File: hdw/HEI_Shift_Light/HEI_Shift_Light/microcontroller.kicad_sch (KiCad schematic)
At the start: 13 parts

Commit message: more schematic progress
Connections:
- net PIC18F_ICSPCLK: now also U?.13 (RA1)
- net PIC18F_ICSPDAT: now also U?.14 (RA0)
- net C2OUT: now reaches U?.10 (RC1)
- net TACH_PULSE: now reaches U?.11 (RC0)
- net TACH_ANALOG: now reaches U?.16 (RB5)
- net USB_UART_TX: now reaches U?.19 (RC7)
- net CLKR: now reaches U?.2 (RA5)
- net USB_UART_RX: now reaches U?.20 (RC6)
- net LED_R: now reaches U?.5 (RC5)
- net LED_G: now reaches U?.6 (RC4)
- net LED_B: now reaches U?.7 (RC3)
- net OPA1OUT: now reaches U?.9 (RC2)
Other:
- note added: "C2IN0+"
- note added: "C2OUT"
- note added: "CLKR"
- note added: "OPA1IN0+/ANB5"
- note added: "OPA1OUT"
- note added: "PWM1S1P1_OUT/CLC1OUT"
- note added: "PWM2S1P1_OUT/CLC2OUT"
- note added: "PWM3S1P1_OUT/CLC3OUT"
- note added: "UART1RX"
- note added: "UART1TX"

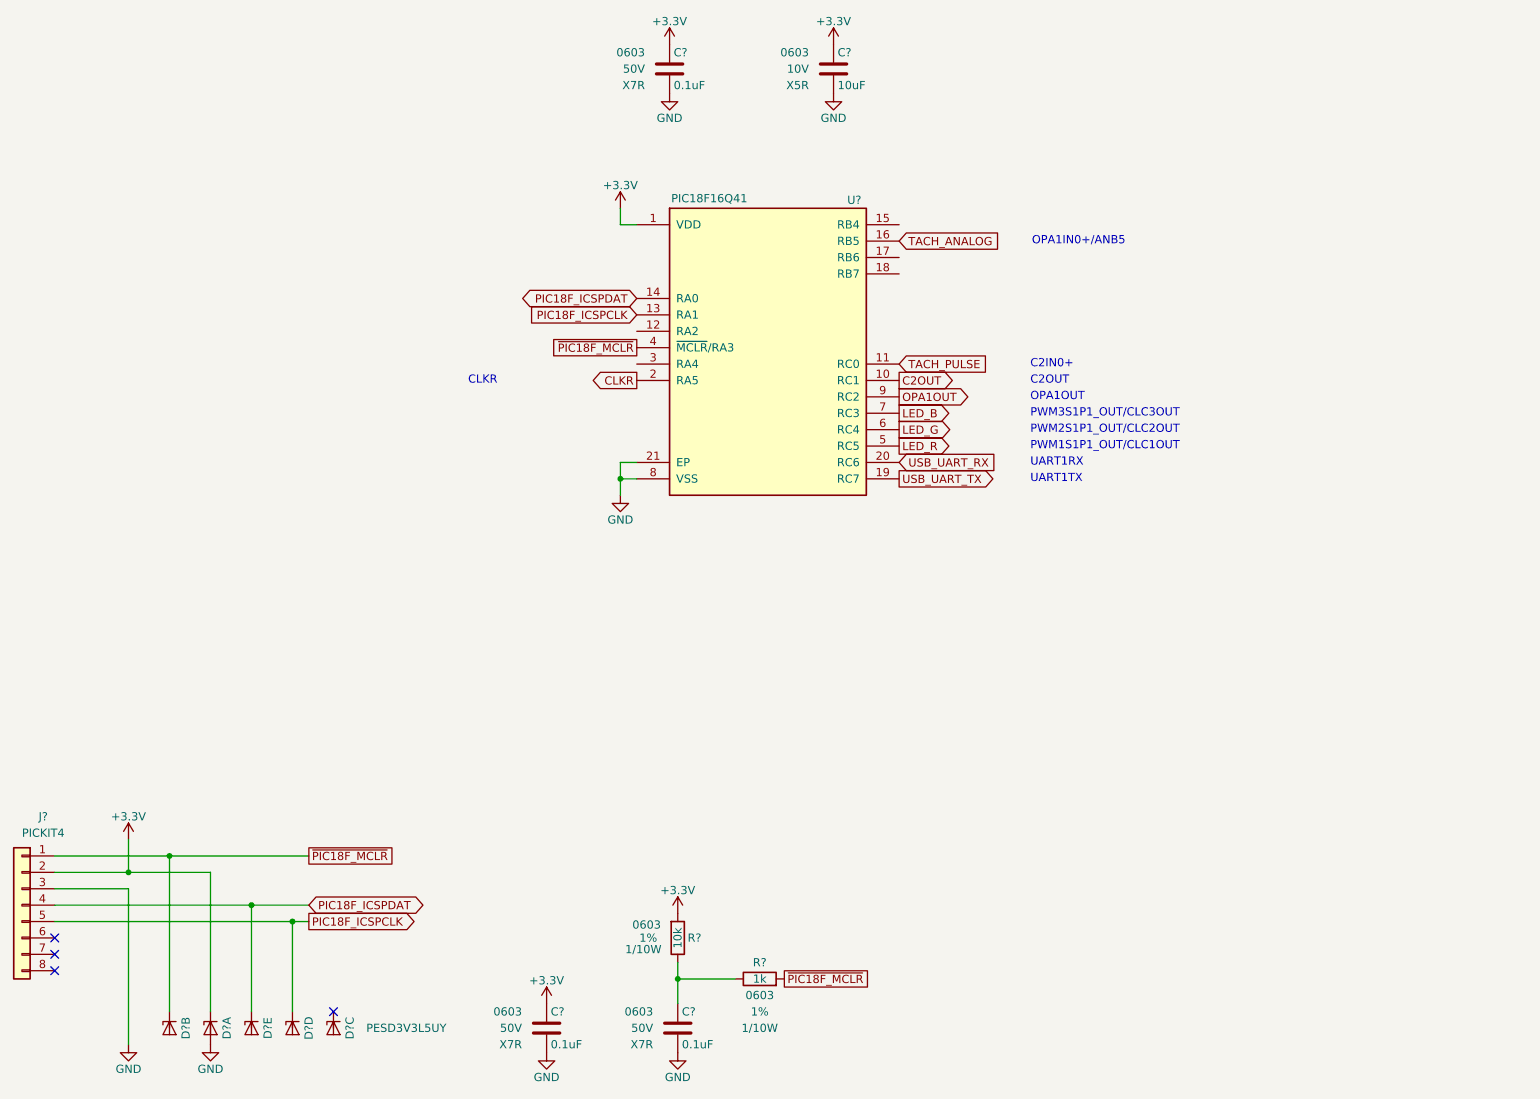
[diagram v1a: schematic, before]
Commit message: populated input protection circuit passive components, updated PIC pinout, added stuff to frequency to voltage converter circuit
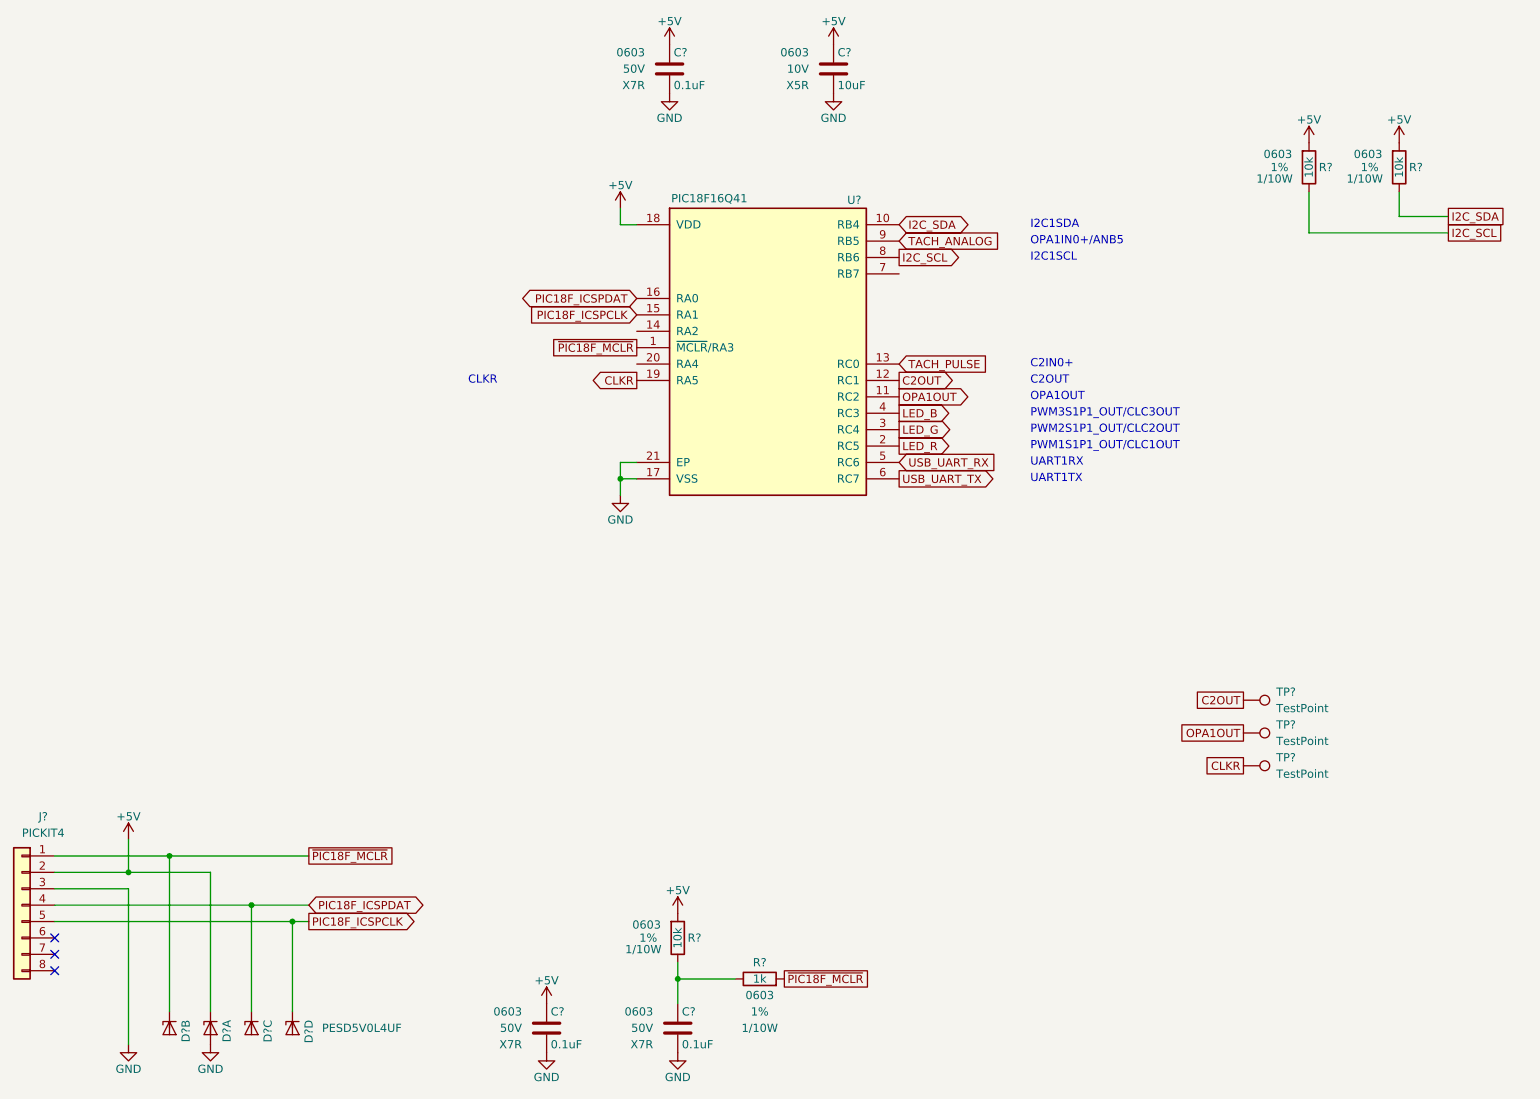
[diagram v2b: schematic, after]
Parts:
- removed D? (x5): PESD3V3L5UY, Package_TO_SOT_SMD:SOT-363_SC-70-6, symbol Power_Protection:PESD3V3L5UY
- added D? (x4): PESD5V0L4UF, Package_TO_SOT_SMD:SOT-886, symbol Power_Protection:PESD5V0L4UF
- added R? (x2): 10k, Resistors_SMD:R_0603, symbol Custom_Library:R_Custom
- added TP? (x3): TestPoint, TestPoint:TestPoint_Pad_D1.0mm, symbol Connector:TestPoint
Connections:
- net C2OUT: now also U?.12 (RC1), TP?.1; no longer U?.10 (RC1)
- net CLKR: now also U?.19 (RA5), TP?.1; no longer U?.2 (RA5)
- net GND: now also U?.17 (VSS), D?.2 (A), D?.5 (A); no longer U?.8 (VSS)
- net LED_B: now also U?.4 (RC3); no longer U?.7 (RC3)
- net LED_G: now also U?.3 (RC4); no longer U?.6 (RC4)
- net LED_R: now also U?.2 (RC5); no longer U?.5 (RC5)
- net OPA1OUT: now also U?.11 (RC2), TP?.1; no longer U?.9 (RC2)
- net PIC18F_ICSPCLK: now also U?.15 (RA1), D?.6 (K4); no longer U?.13 (RA1)
- net PIC18F_ICSPDAT: now also U?.16 (RA0), D?.4 (K3); no longer U?.14 (RA0)
- net TACH_ANALOG: now also U?.9 (RB5); no longer U?.16 (RB5)
- net TACH_PULSE: now also U?.13 (RC0); no longer U?.11 (RC0)
- net USB_UART_RX: now also U?.5 (RC6); no longer U?.20 (RC6)
- net USB_UART_TX: now also U?.6 (RC7); no longer U?.19 (RC7)
- net ~{PIC18F_MCLR}: now also U?.1 (~{MCLR}/RA3), D?.3 (K2); no longer U?.4 (~{MCLR}/RA3)
- net +5V: now reaches U?.18 (VDD)
- net +5V: now also C?.1, C?.1, C?.1, J?.2 (Pin_2), R?.1, D?.1 (K1), R?.1, R?.1
- removed net +3.3V: C?.1, C?.1, C?.1, J?.2 (Pin_2), R?.1, U?.1 (VDD)
- new net I2C_SCL: R?.2, U?.8 (RB6)
- new net I2C_SDA: R?.2, U?.10 (RB4)
- no-connect marks 4 -> 3
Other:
- note added: "I2C1SCL"
- note added: "I2C1SDA"

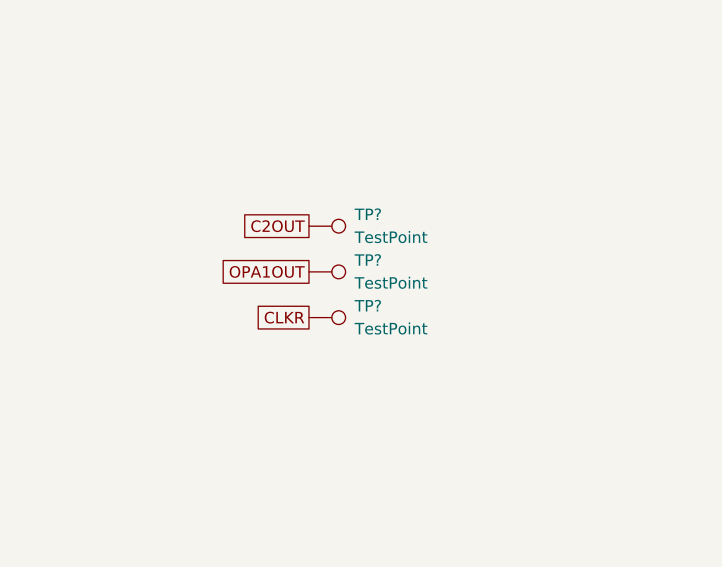
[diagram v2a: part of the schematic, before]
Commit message: added more shit, RGD LED, LC input filter
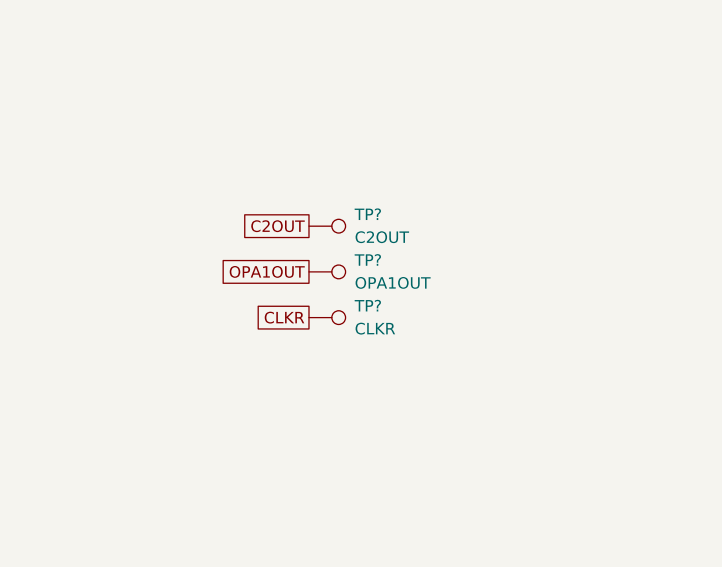
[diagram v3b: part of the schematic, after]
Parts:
- TP?: value TestPoint -> OPA1OUT
- TP?: value TestPoint -> C2OUT
- TP?: value TestPoint -> CLKR
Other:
- company: (none) -> Drew Maatman
- title: (none) -> HEI Shift Light
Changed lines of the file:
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@@
 	(generator_version "10.0")
 	(paper "A")
+	(title_block
+		(title "HEI Shift Light")
+		(date "2026-05-29")
+		(rev "A")
+		(company "Drew Maatman")
+	)
 	(text "C2OUT"
 		(exclude_from_sim no)
@@
 		(in_pos_files yes)
 		(dnp no)
-		(property "Reference" "#PWR041"
+		(property "Reference" "#PWR?"
 			(at 217.17 53.34 0)
 			(hide yes)
@@
 			(project "HEI_Shift_Light"
 				(path "/288c8230-69eb-4ad9-929d-f4630114196f/5c9f220d-57b1-4b37-ac12-25339229b122"
-					(reference "#PWR041")
+					(reference "#PWR?")
 					(unit 1)
 				)
@@
 		(in_pos_files yes)
 		(dnp no)
-		(property "Reference" "#PWR027"
+		(property "Reference" "#PWR?"
 			(at 118.11 38.1 0)
 			(hide yes)
@@
 			(project "HEI_Shift_Light"
 				(path "/288c8230-69eb-4ad9-929d-f4630114196f/5c9f220d-57b1-4b37-ac12-25339229b122"
-					(reference "#PWR027")
+					(reference "#PWR?")
 					(unit 1)
 				)
@@
 			)
 		)
-		(property "Value" "TestPoint"
+		(property "Value" "OPA1OUT"
 			(at 212.09 142.2399 90)
 			(show_name no)
@@
 		(in_pos_files yes)
 		(dnp no)
-		(property "Reference" "#PWR031"
+		(property "Reference" "#PWR?"
 			(at 119.38 172.72 0)
 			(hide yes)
@@
 			(project "HEI_Shift_Light"
 				(path "/288c8230-69eb-4ad9-929d-f4630114196f/5c9f220d-57b1-4b37-ac12-25339229b122"
-					(reference "#PWR031")
+					(reference "#PWR?")
 					(unit 1)
 				)
@@
 			)
 		)
-		(property "Value" "TestPoint"
+		(property "Value" "C2OUT"
 			(at 212.09 137.1599 90)
 			(show_name no)
@@
 		(in_pos_files yes)
 		(dnp no)
-		(property "Reference" "#PWR042"
+		(property "Reference" "#PWR?"
 			(at 231.14 53.34 0)
 			(hide yes)
@@
 			(project "HEI_Shift_Light"
 				(path "/288c8230-69eb-4ad9-929d-f4630114196f/5c9f220d-57b1-4b37-ac12-25339229b122"
-					(reference "#PWR042")
+					(reference "#PWR?")
 					(unit 1)
 				)
@@
 		(in_pos_files yes)
 		(dnp no)
-		(property "Reference" "#PWR030"
+		(property "Reference" "#PWR?"
 			(at 99.06 186.69 0)
 			(hide yes)
@@
 			(project "HEI_Shift_Light"
 				(path "/288c8230-69eb-4ad9-929d-f4630114196f/5c9f220d-57b1-4b37-ac12-25339229b122"
-					(reference "#PWR030")
+					(reference "#PWR?")
 					(unit 1)
 				)
@@
 		(in_pos_files yes)
 		(dnp no)
-		(property "Reference" "#PWR029"
+		(property "Reference" "#PWR?"
 			(at 34.29 161.29 0)
 			(hide yes)
@@
 			(project "HEI_Shift_Light"
 				(path "/288c8230-69eb-4ad9-929d-f4630114196f/5c9f220d-57b1-4b37-ac12-25339229b122"
-					(reference "#PWR029")
+					(reference "#PWR?")
 					(unit 1)
 				)
@@
 		(in_pos_files yes)
 		(dnp no)
-		(property "Reference" "#PWR028"
+		(property "Reference" "#PWR?"
 			(at 143.51 38.1 0)
 			(hide yes)
@@
 			(project "HEI_Shift_Light"
 				(path "/288c8230-69eb-4ad9-929d-f4630114196f/5c9f220d-57b1-4b37-ac12-25339229b122"
-					(reference "#PWR028")
+					(reference "#PWR?")
 					(unit 1)
 				)
@@
 		(in_pos_files yes)
 		(dnp no)
-		(property "Reference" "#PWR026"
+		(property "Reference" "#PWR?"
 			(at 110.49 63.5 0)
 			(hide yes)
@@
 			(project "HEI_Shift_Light"
 				(path "/288c8230-69eb-4ad9-929d-f4630114196f/5c9f220d-57b1-4b37-ac12-25339229b122"
-					(reference "#PWR026")
+					(reference "#PWR?")
 					(unit 1)
 				)
@@
 			)
 		)
-		(property "Value" "TestPoint"
+		(property "Value" "CLKR"
 			(at 212.09 147.3199 90)
 			(show_name no)
